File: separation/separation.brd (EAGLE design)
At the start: 0 parts

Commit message: add rp2040
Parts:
- added JP2, JP4: (no value), microbuilder:1X07_OVAL
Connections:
- new net +3V3: JP4.5
- new net A0: JP2.1
- new net A1: JP2.2
- new net A2: JP2.3
- new net A3: JP2.4
- new net GND: JP4.6
- new net MISO: JP4.3
- new net MOSI: JP4.4
- new net RX: JP4.1
- new net SCK: JP4.2
- new net SCL: JP2.6
- new net SDA: JP2.5
- new net TX: JP2.7
- new net VCC: JP4.7

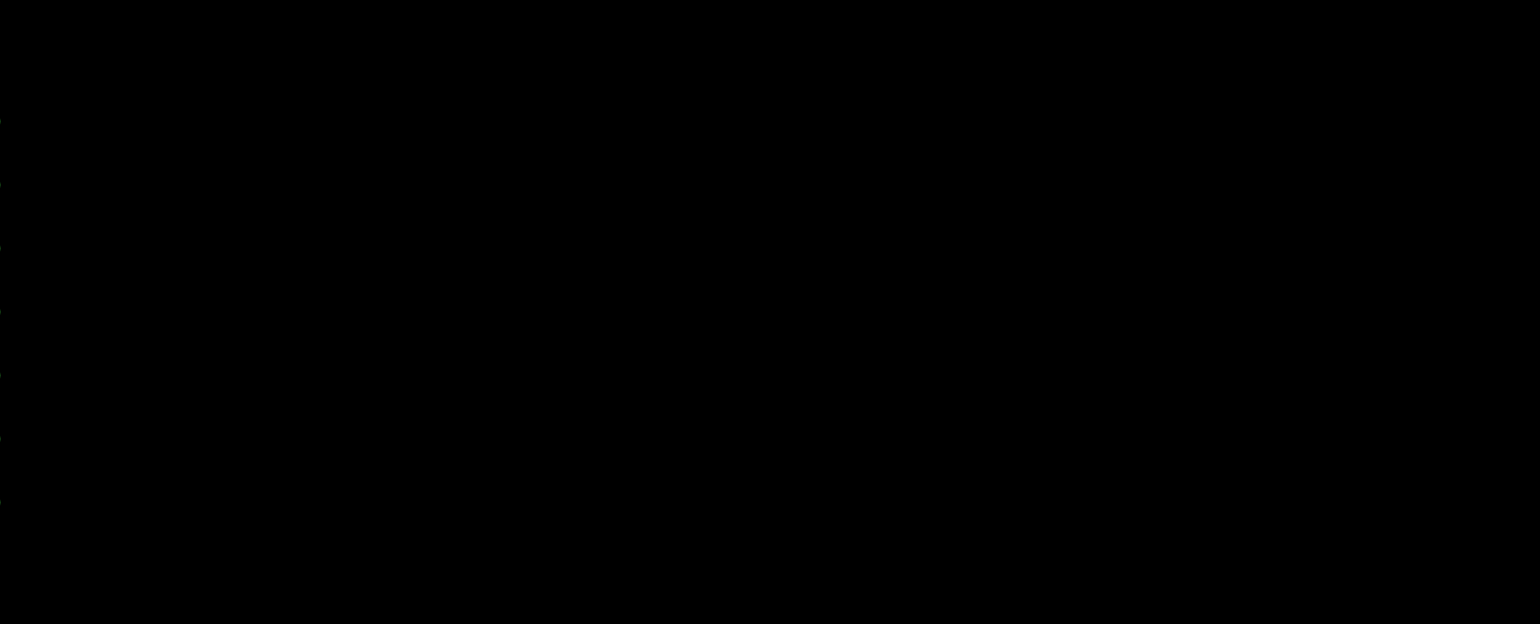
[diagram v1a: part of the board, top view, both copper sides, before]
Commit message: add 2x dps
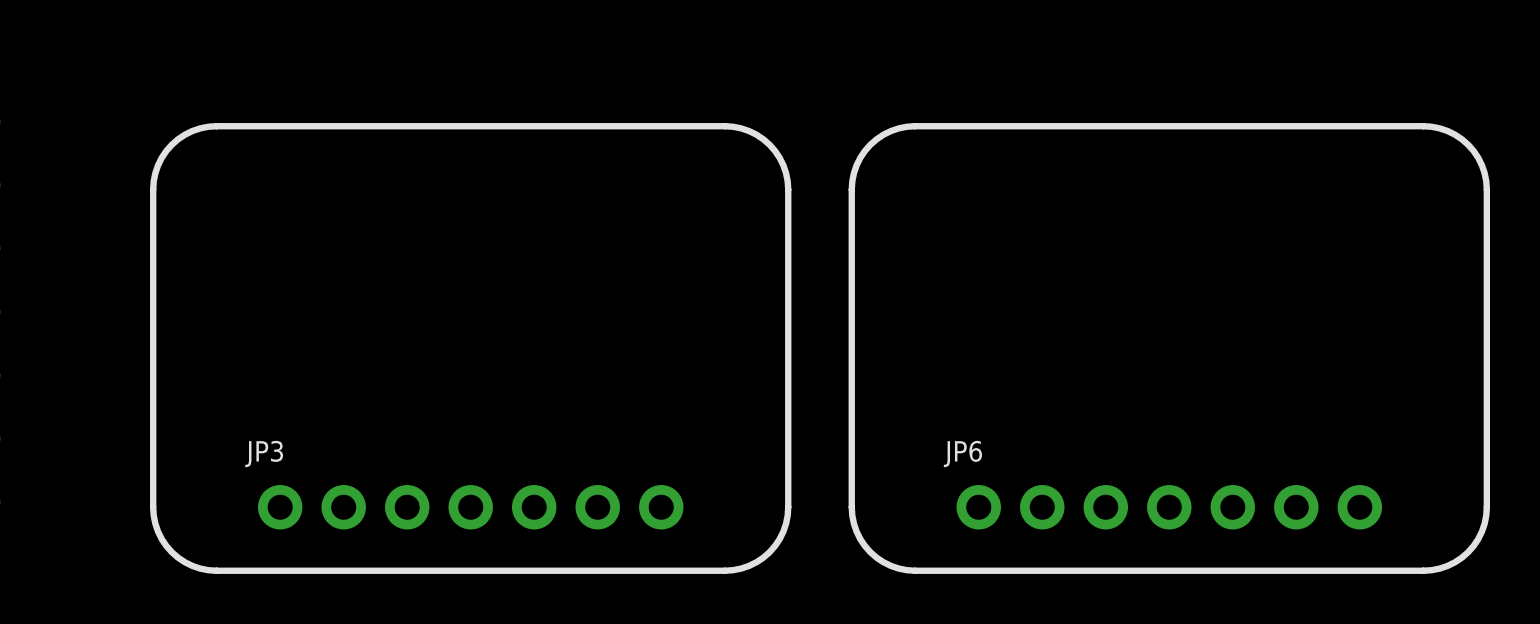
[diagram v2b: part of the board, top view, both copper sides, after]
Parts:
- added JP3, JP6: (no value), microbuilder:1X07_ROUND_70
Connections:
- new net 3.3V: JP3.2, JP6.2
- new net CS: JP3.7, JP6.7
- new net SDO/ADR: JP3.5
- new net SDO/ADR_2: JP6.5
- net GND: now also JP3.3, JP6.3
- net SCL: now also JP3.4, JP6.4
- net SDA: now also JP3.6, JP6.6
- net VCC: now also JP3.1, JP6.1
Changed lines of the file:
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@@
 <wire x1="54.61" y1="63.627" x2="56.388" y2="63.627" width="1.524" layer="29"/>
 <wire x1="54.61" y1="61.087" x2="56.388" y2="61.087" width="1.524" layer="29"/>
+<wire x1="62.23" y1="73.66" x2="62.23" y2="60.96" width="0.254" layer="21"/>
+<wire x1="62.23" y1="60.96" x2="64.77" y2="58.42" width="0.254" layer="21" curve="90"/>
+<wire x1="64.77" y1="58.42" x2="85.09" y2="58.42" width="0.254" layer="21"/>
+<wire x1="85.09" y1="58.42" x2="87.63" y2="60.96" width="0.254" layer="21" curve="90"/>
+<wire x1="87.63" y1="60.96" x2="87.63" y2="73.66" width="0.254" layer="21"/>
+<wire x1="87.63" y1="73.66" x2="85.09" y2="76.2" width="0.254" layer="21" curve="90"/>
+<wire x1="85.09" y1="76.2" x2="64.77" y2="76.2" width="0.254" layer="21"/>
+<wire x1="64.77" y1="76.2" x2="62.23" y2="73.66" width="0.254" layer="21" curve="90"/>
+<wire x1="90.17" y1="73.66" x2="90.17" y2="60.96" width="0.254" layer="21"/>
+<wire x1="90.17" y1="60.96" x2="92.71" y2="58.42" width="0.254" layer="21" curve="90"/>
+<wire x1="92.71" y1="58.42" x2="113.03" y2="58.42" width="0.254" layer="21"/>
+<wire x1="113.03" y1="58.42" x2="115.57" y2="60.96" width="0.254" layer="21" curve="90"/>
+<wire x1="115.57" y1="60.96" x2="115.57" y2="73.66" width="0.254" layer="21"/>
+<wire x1="115.57" y1="73.66" x2="113.03" y2="76.2" width="0.254" layer="21" curve="90"/>
+<wire x1="113.03" y1="76.2" x2="92.71" y2="76.2" width="0.254" layer="21"/>
+<wire x1="92.71" y1="76.2" x2="90.17" y2="73.66" width="0.254" layer="21" curve="90"/>
 </plain>
 <attributes>
@@
 <class number="0" name="default" width="0" drill="0">
 </class>
-<class number="1" name="power" width="0.3048" drill="0">
+<class number="1" name="highpower" width="0.3048" drill="0.4826">
+</class>
+<class number="2" name="lowpower" width="0.3048" drill="0.4826">
 </class>
 </classes>
@@
 <attribute name="VALUE" x="57.785" y="59.8805" size="0.4064" layer="27" ratio="10" rot="R90"/>
 </element>
+<element name="JP3" library="microbuilder" package="1X07_ROUND_70" value="" x="74.93" y="60.96" smashed="yes">
+<attribute name="NAME" x="65.9638" y="62.7888" size="0.8128" layer="25" ratio="18"/>
+<attribute name="VALUE" x="66.04" y="57.785" size="0.4064" layer="27" ratio="10"/>
+</element>
+<element name="JP6" library="microbuilder" package="1X07_ROUND_70" value="" x="102.87" y="60.96" smashed="yes">
+<attribute name="NAME" x="93.9038" y="62.7888" size="0.8128" layer="25" ratio="18"/>
+<attribute name="VALUE" x="93.98" y="57.785" size="0.4064" layer="27" ratio="10"/>
+</element>
 </elements>
 <signals>
 <signal name="GND" class="1">
 <contactref element="JP4" pad="6"/>
+<contactref element="JP3" pad="3"/>
+<contactref element="JP6" pad="3"/>
+<wire x1="72.39" y1="60.96" x2="100.33" y2="60.96" width="0" layer="19" extent="1-1"/>
+<wire x1="54.61" y1="73.8505" x2="72.39" y2="60.96" width="0" layer="19" extent="1-1"/>
 </signal>
 <signal name="A0">
@@
 <signal name="SDA">
 <contactref element="JP2" pad="5"/>
+<contactref element="JP3" pad="6"/>
+<contactref element="JP6" pad="6"/>
+<wire x1="80.01" y1="60.96" x2="107.95" y2="60.96" width="0" layer="19" extent="1-1"/>
+<wire x1="39.37" y1="66.2305" x2="80.01" y2="60.96" width="0" layer="19" extent="1-1"/>
 </signal>
 <signal name="SCL">
 <contactref element="JP2" pad="6"/>
+<contactref element="JP3" pad="4"/>
+<contactref element="JP6" pad="4"/>
+<wire x1="74.93" y1="60.96" x2="102.87" y2="60.96" width="0" layer="19" extent="1-1"/>
+<wire x1="39.37" y1="63.6905" x2="74.93" y2="60.96" width="0" layer="19" extent="1-1"/>
 </signal>
 <signal name="VCC" class="1">
 <contactref element="JP4" pad="7"/>
+<contactref element="JP3" pad="1"/>
+<contactref element="JP6" pad="1"/>
+<wire x1="67.31" y1="60.96" x2="95.25" y2="60.96" width="0" layer="19" extent="1-1"/>
+<wire x1="54.61" y1="76.3905" x2="67.31" y2="60.96" width="0" layer="19" extent="1-1"/>
 </signal>
 <signal name="+3V3">
@@
 <contactref element="JP4" pad="1"/>
 </signal>
+<signal name="3.3V" class="2">
+<contactref element="JP3" pad="2"/>
+<contactref element="JP6" pad="2"/>
+<wire x1="69.85" y1="60.96" x2="97.79" y2="60.96" width="0" layer="19" extent="1-1"/>
+</signal>
+<signal name="SDO/ADR">
+<contactref element="JP3" pad="5"/>
+</signal>
+<signal name="CS">
+<contactref element="JP3" pad="7"/>
+<contactref element="JP6" pad="7"/>
+<wire x1="82.55" y1="60.96" x2="110.49" y2="60.96" width="0" layer="19" extent="1-1"/>
+</signal>
+<signal name="SDO/ADR_2">
+<contactref element="JP6" pad="5"/>
+</signal>
 </signals>

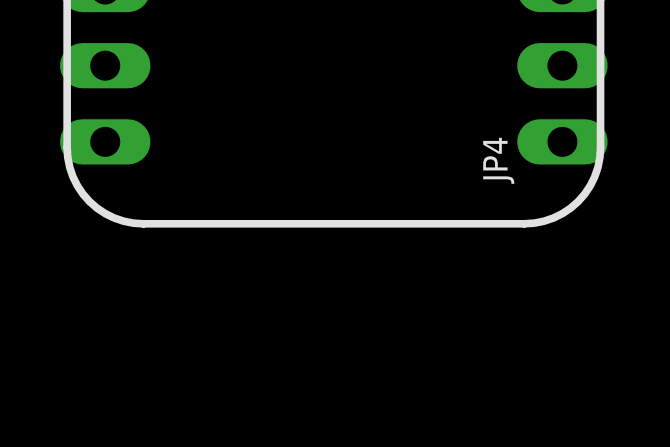
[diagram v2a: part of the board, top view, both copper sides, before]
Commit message: add regulator
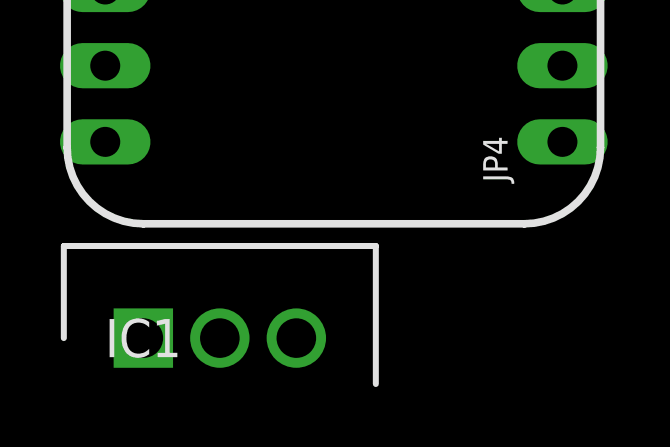
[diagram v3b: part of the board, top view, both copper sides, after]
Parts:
- added IC1: L7805ACV, SamacSys_Parts:TO255P460X1020X2008-3P
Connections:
- new net VBAT: IC1.1
- net GND: now also IC1.2
- net VCC: now also IC1.3
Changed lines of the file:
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@@
 <attribute name="VALUE" x="93.98" y="57.785" size="0.4064" layer="27" ratio="10"/>
+</element>
+<element name="IC1" library="SamacSys_Parts" package="TO255P460X1020X2008-3P" value="L7805ACV" x="40.64" y="54.61" smashed="yes">
+<attribute name="ALLIED_NUMBER" value="70013701" x="40.64" y="54.61" size="1.778" layer="27" font="vector" ratio="15" display="off"/>
+<attribute name="DESCRIPTION" value="Linear voltage regulator,L7805ACV 5V 1A STMicroelectronics L7805ACV, Single Linear Voltage Regulator, 1A 5 V, 2%, 3-Pin TO-220" x="40.64" y="54.61" size="1.778" layer="27" font="vector" ratio="15" display="off"/>
+<attribute name="HEIGHT" value="4.6mm" x="40.64" y="54.61" size="1.778" layer="27" font="vector" ratio="15" display="off"/>
+<attribute name="MANUFACTURER_NAME" value="STMicroelectronics" x="40.64" y="54.61" size="1.778" layer="27" font="vector" ratio="15" display="off"/>
+<attribute name="MANUFACTURER_PART_NUMBER" value="L7805ACV" x="40.64" y="54.61" size="1.778" layer="27" font="vector" ratio="15" display="off"/>
+<attribute name="NAME" x="40.64" y="54.61" size="1.27" layer="25" align="center"/>
+<attribute name="RS_PART_NUMBER" value="2988508P" x="40.64" y="54.61" size="1.778" layer="27" font="vector" ratio="15" display="off"/>
+<attribute name="RS_PRICE-STOCK" value="http://uk.rs-online.com/web/p/products/2988508P" x="40.64" y="54.61" size="1.778" layer="27" font="vector" ratio="15" display="off"/>
+<attribute name="VALUE" x="40.64" y="54.61" size="1.27" layer="27" align="center"/>
 </element>
 </elements>
@@
 <contactref element="JP3" pad="3"/>
 <contactref element="JP6" pad="3"/>
+<contactref element="IC1" pad="2"/>
 <wire x1="72.39" y1="60.96" x2="100.33" y2="60.96" width="0" layer="19" extent="1-1"/>
 <wire x1="54.61" y1="73.8505" x2="72.39" y2="60.96" width="0" layer="19" extent="1-1"/>
+<wire x1="43.19" y1="54.61" x2="54.61" y2="73.8505" width="0" layer="19" extent="1-1"/>
 </signal>
 <signal name="A0">
@@
 <contactref element="JP3" pad="1"/>
 <contactref element="JP6" pad="1"/>
+<contactref element="IC1" pad="3"/>
 <wire x1="67.31" y1="60.96" x2="95.25" y2="60.96" width="0" layer="19" extent="1-1"/>
 <wire x1="54.61" y1="76.3905" x2="67.31" y2="60.96" width="0" layer="19" extent="1-1"/>
+<wire x1="45.74" y1="54.61" x2="67.31" y2="60.96" width="0" layer="19" extent="1-1"/>
 </signal>
 <signal name="+3V3">
@@
 <contactref element="JP6" pad="5"/>
 </signal>
+<signal name="VBAT">
+<contactref element="IC1" pad="1"/>
+</signal>
 </signals>
